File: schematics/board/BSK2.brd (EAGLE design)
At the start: 82 x 100 mm, 26 parts

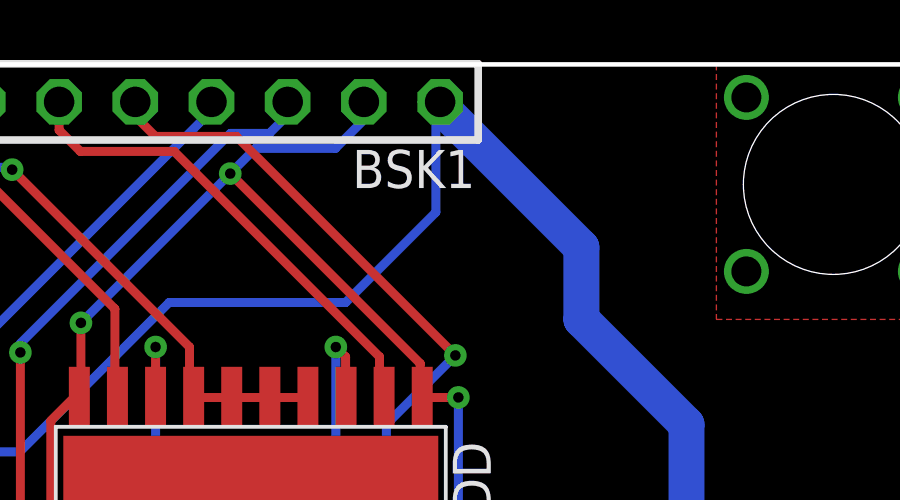
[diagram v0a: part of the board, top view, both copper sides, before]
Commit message: Подписаны разъемы на платах
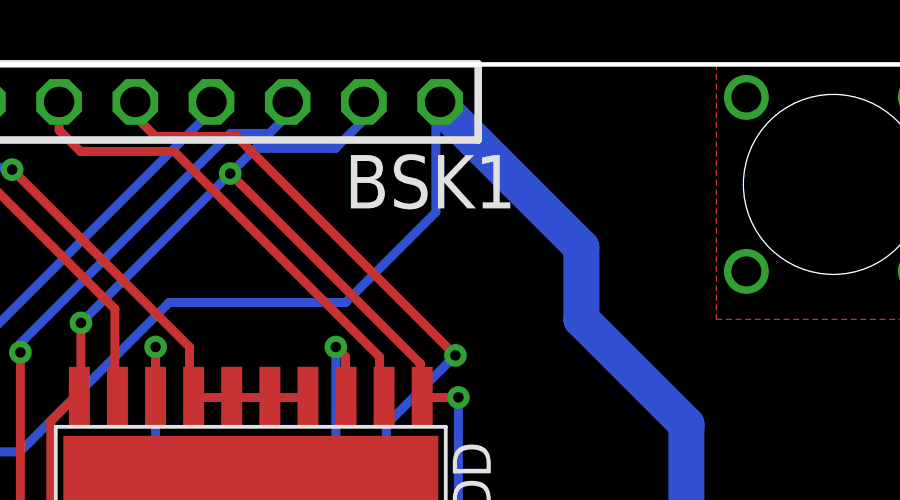
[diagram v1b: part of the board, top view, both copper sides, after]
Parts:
- renumbered BSK1 to TO_BSK1
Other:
- board text added: "BSK1"
- board text added: "to BSK1"
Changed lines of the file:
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@@
 <text x="52.2" y="1.9" size="1.778" layer="26" rot="MR0">BSK2 "Концерн ИТС"</text>
 <circle x="41" y="50" radius="15.25" width="0.2" layer="20"/>
+<text x="54.7" y="95.2" size="1.778" layer="25">BSK1</text>
+<text x="63.5" y="95" size="1.778" layer="26" rot="MR0">to BSK1</text>
 </plain>
 <attributes>
@@
 <attribute name="VALUE" x="23.310459375" y="27.30414375" size="1.27" layer="27" rot="R135"/>
 </element>
-<element name="BSK1" library="pinheadCS" package="1X08" value="" x="49" y="98.75" smashed="yes">
-<attribute name="NAME" x="54.9638" y="95.8788" size="1.27" layer="25" ratio="10"/>
+<element name="TO_BSK1" library="pinheadCS" package="1X08" value="" x="49" y="98.75" smashed="yes">
 <attribute name="VALUE" x="38.84" y="95.575" size="1.27" layer="27"/>
 </element>
@@
 <contactref element="U$8" pad="17"/>
 <contactref element="U$14" pad="67"/>
-<contactref element="BSK1" pad="1"/>
+<contactref element="TO_BSK1" pad="1"/>
 <wire x1="41.6208" y1="86.6346" x2="38.5802" y2="89.6752" width="0.3" layer="1"/>
 <wire x1="41.6208" y1="77.1342" x2="41.6208" y2="86.6346" width="0.3" layer="1"/>
@@
 <contactref element="U$8" pad="11"/>
 <contactref element="U$8" pad="20"/>
-<contactref element="BSK1" pad="7"/>
+<contactref element="TO_BSK1" pad="7"/>
 <contactref element="U$5" pad="3"/>
 <wire x1="57.4548" y1="88.8966" x2="57.295" y2="88.92" width="0.3" layer="1"/>
@@
 <signal name="1W">
 <contactref element="U$5" pad="4"/>
-<contactref element="BSK1" pad="6"/>
+<contactref element="TO_BSK1" pad="6"/>
 <wire x1="35.88" y1="71.875" x2="35.005" y2="71" width="0.3" layer="1"/>
 <wire x1="35.005" y1="71" x2="33.7" y2="71" width="0.3" layer="1"/>
@@
 </signal>
 <signal name="B2_KEM+">
-<contactref element="BSK1" pad="3"/>
+<contactref element="TO_BSK1" pad="3"/>
 <contactref element="U$8" pad="2"/>
 <wire x1="55.8714" y1="89.1228" x2="55.8714" y2="90.2538" width="0.3" layer="1"/>
@@
 </signal>
 <signal name="B2_KEM-">
-<contactref element="BSK1" pad="2"/>
+<contactref element="TO_BSK1" pad="2"/>
 <contactref element="U$8" pad="9"/>
 <wire x1="47.135" y1="88.92" x2="47.0496" y2="89.1228" width="0.3" layer="1"/>
@@
 </signal>
 <signal name="B2_KHEAT">
-<contactref element="BSK1" pad="4"/>
+<contactref element="TO_BSK1" pad="4"/>
 <contactref element="U$8" pad="19"/>
 <wire x1="56.025" y1="79.32" x2="56.025" y2="77.475" width="0.3" layer="1"/>
@@
 </signal>
 <signal name="B2_KVCC">
-<contactref element="BSK1" pad="5"/>
+<contactref element="TO_BSK1" pad="5"/>
 <contactref element="R10" pad="1"/>
 <contactref element="R11" pad="1"/>
@@
 <signal name="BUS+">
 <contactref element="R19" pad="2"/>
-<contactref element="BSK1" pad="8"/>
+<contactref element="TO_BSK1" pad="8"/>
 <contactref element="U$3" pad="1"/>
 <contactref element="U$3" pad="2"/>

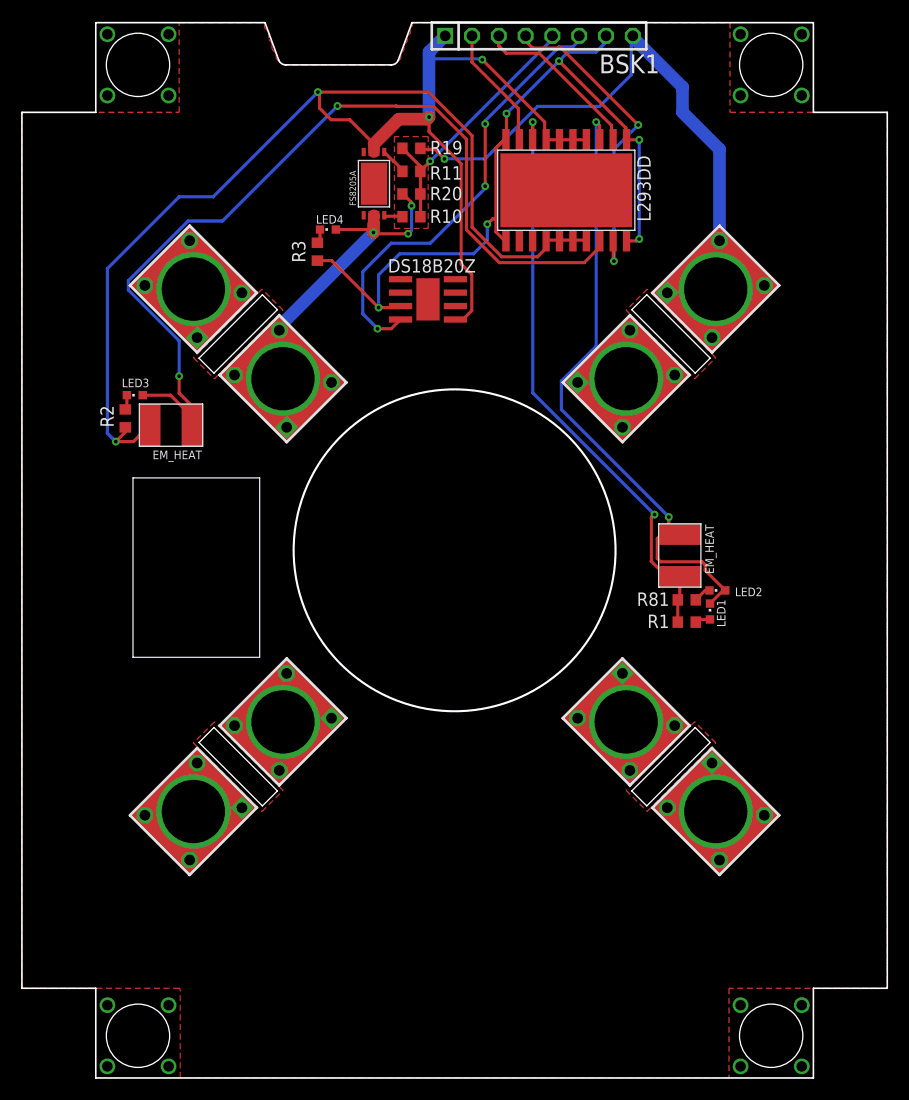
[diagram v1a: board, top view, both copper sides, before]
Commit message: Внёс незначительные правки на платах. Но пока не везде
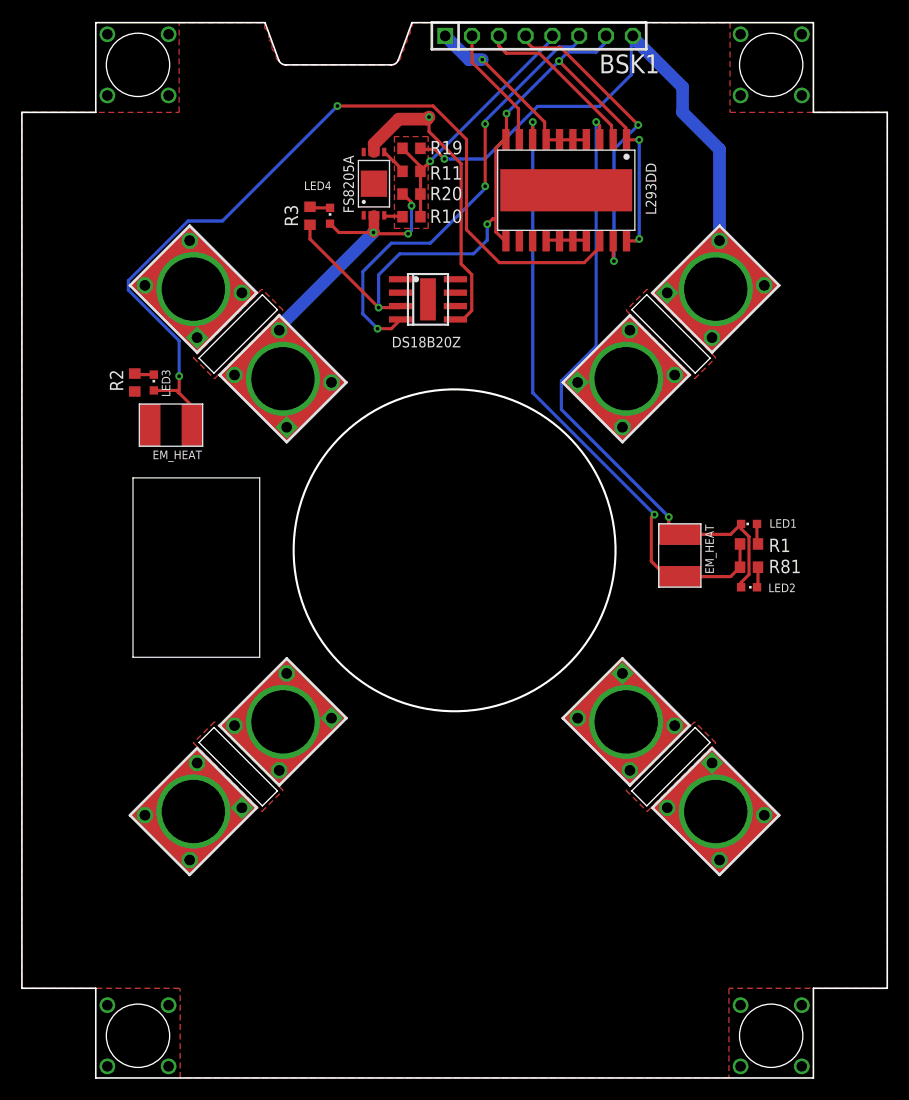
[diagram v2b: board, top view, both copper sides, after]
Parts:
- removed U$14: FS8205A, CanCubeSat:FS8205A
- added FS8205A: FS8205A+, CanCubeSat:FS8205A+
- moved R1 9.46 mm to (68.9, 50.6)
- moved LED1 9.09 mm to (68.9, 52.5), turned to 90 degrees
- moved R81 6.66 mm to (68.9, 48.4)
- moved R2 3.52 mm to (10.7, 65.9)
- moved R3 3.47 mm to (27.3, 81.7)
- moved LED2 3.01 mm to (68.9, 46.5), turned to 270 degrees
- moved LED3 2.16 mm to (12.5, 65.9), turned to 0 degrees
- moved LED4 1.32 mm to (29.2, 81.7), turned to 0 degrees
- renumbered U$5 to DS18B20Z, U$8 to L293DD
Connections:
- removed net HEAT: DS18B20Z.HEAT, L293DD.HEAT, U$14.HEAT
- net BUS-: now also FS8205A.23; no longer U$14.23
- net GND: now also DS18B20Z.HEAT, FS8205A.67, FS8205A.HEAT, L293DD.HEAT; no longer U$14.67
- net N$8: now also FS8205A.4; no longer U$14.4
- net N$9: now also FS8205A.5; no longer U$14.5
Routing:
- net GND: track 151.7 -> 52.2 mm, vias 4 -> 2
- net N$2: track 55.9 -> 59.8 mm
- net N$3: track 86.4 -> 82.6 mm
- net 5V: track 74.8 -> 77.7 mm
- net N$1: track 61.0 -> 59.7 mm
- net BUS-: track 44.6 -> 45.4 mm
- net N$25: track 1.35 -> 1.94 mm
- added copper zone on layer 1, net GND
- removed copper zone on layer 1, net HEAT

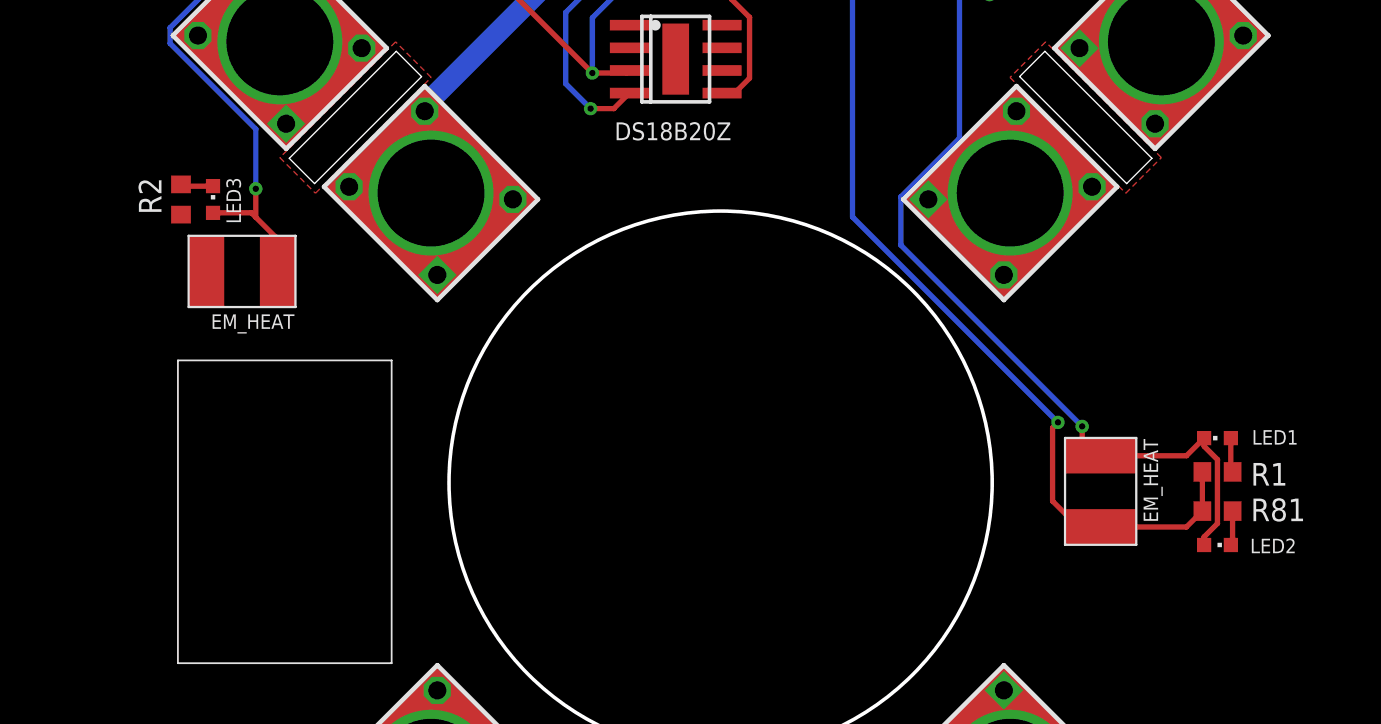
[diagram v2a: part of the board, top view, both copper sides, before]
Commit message: Внесены косметические изменения на БСК2 и БСК3
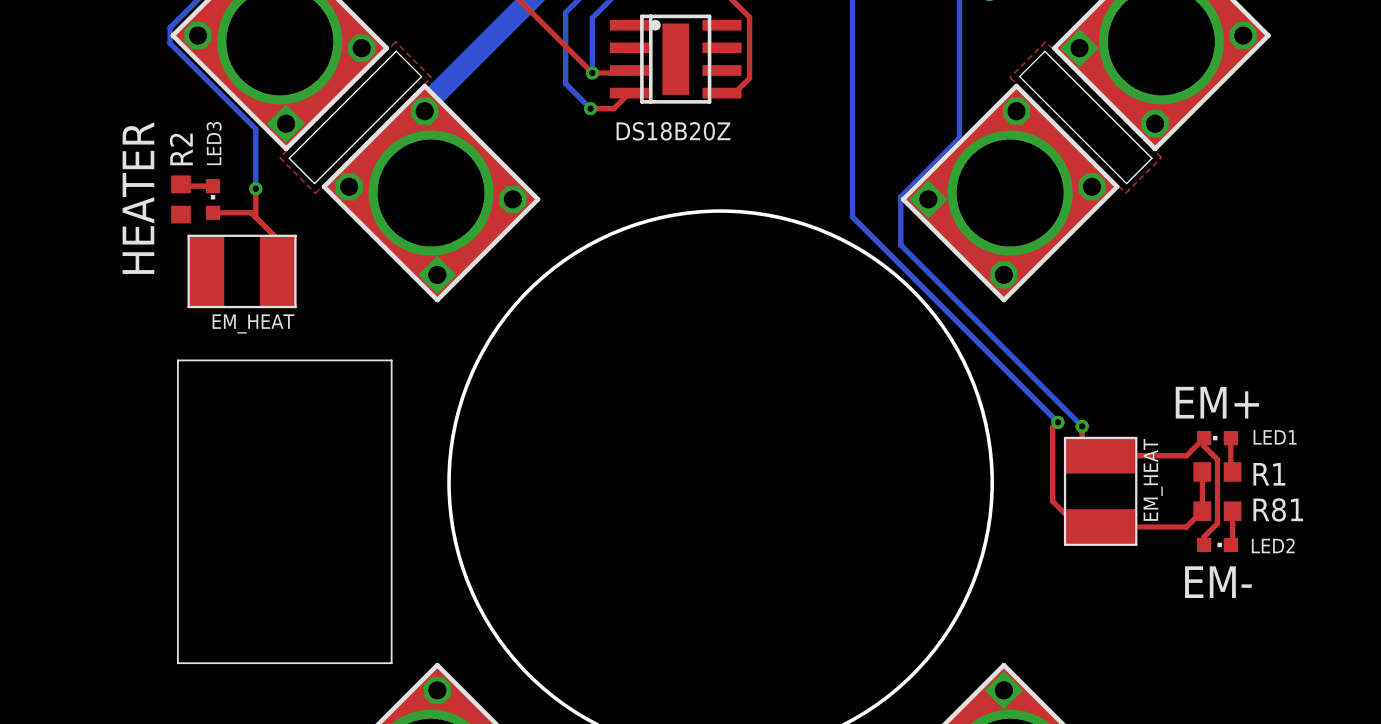
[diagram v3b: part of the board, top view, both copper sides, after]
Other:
- board text added: "EM+"
- board text added: "EM-"
- board text added: "HEATER"
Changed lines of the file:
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@@
 <?xml version="1.0" encoding="utf-8"?>
 <!DOCTYPE eagle SYSTEM "eagle.dtd">
-<eagle version="9.5.1">
+<eagle version="9.4.2">
 <drawing>
 <settings>
@@
 <layer number="14" name="Route14" color="22" fill="1" visible="no" active="no"/>
 <layer number="15" name="Route15" color="23" fill="1" visible="no" active="no"/>
-<layer number="16" name="Bottom" color="1" fill="1" visible="yes" active="yes"/>
+<layer number="16" name="Bottom" color="1" fill="1" visible="no" active="yes"/>
 <layer number="17" name="Pads" color="2" fill="1" visible="yes" active="yes"/>
 <layer number="18" name="Vias" color="2" fill="1" visible="yes" active="yes"/>
@@
 <layer number="20" name="Dimension" color="24" fill="1" visible="yes" active="yes"/>
 <layer number="21" name="tPlace" color="7" fill="1" visible="yes" active="yes"/>
-<layer number="22" name="bPlace" color="7" fill="1" visible="yes" active="yes"/>
+<layer number="22" name="bPlace" color="7" fill="1" visible="no" active="yes"/>
 <layer number="23" name="tOrigins" color="15" fill="1" visible="yes" active="yes"/>
-<layer number="24" name="bOrigins" color="15" fill="1" visible="yes" active="yes"/>
+<layer number="24" name="bOrigins" color="15" fill="1" visible="no" active="yes"/>
 <layer number="25" name="tNames" color="7" fill="1" visible="yes" active="yes"/>
-<layer number="26" name="bNames" color="7" fill="1" visible="yes" active="yes"/>
+<layer number="26" name="bNames" color="7" fill="1" visible="no" active="yes"/>
 <layer number="27" name="tValues" color="7" fill="1" visible="no" active="yes"/>
-<layer number="28" name="bValues" color="7" fill="1" visible="yes" active="yes"/>
-<layer number="29" name="tStop" color="7" fill="3" visible="yes" active="yes"/>
+<layer number="28" name="bValues" color="7" fill="1" visible="no" active="yes"/>
+<layer number="29" name="tStop" color="7" fill="3" visible="no" active="yes"/>
 <layer number="30" name="bStop" color="7" fill="6" visible="no" active="yes"/>
 <layer number="31" name="tCream" color="7" fill="4" visible="no" active="yes"/>
@@
 <layer number="38" name="bTest" color="7" fill="1" visible="no" active="yes"/>
 <layer number="39" name="tKeepout" color="4" fill="11" visible="yes" active="yes"/>
-<layer number="40" name="bKeepout" color="1" fill="11" visible="yes" active="yes"/>
+<layer number="40" name="bKeepout" color="1" fill="11" visible="no" active="yes"/>
 <layer number="41" name="tRestrict" color="4" fill="10" visible="yes" active="yes"/>
-<layer number="42" name="bRestrict" color="1" fill="10" visible="yes" active="yes"/>
-<layer number="43" name="vRestrict" color="2" fill="10" visible="yes" active="yes"/>
+<layer number="42" name="bRestrict" color="1" fill="10" visible="no" active="yes"/>
+<layer number="43" name="vRestrict" color="2" fill="10" visible="no" active="yes"/>
 <layer number="44" name="Drills" color="7" fill="1" visible="no" active="yes"/>
-<layer number="45" name="Holes" color="7" fill="1" visible="yes" active="yes"/>
+<layer number="45" name="Holes" color="7" fill="1" visible="no" active="yes"/>
 <layer number="46" name="Milling" color="3" fill="1" visible="no" active="yes"/>
 <layer number="47" name="Measures" color="7" fill="1" visible="no" active="yes"/>
-<layer number="48" name="Document" color="7" fill="1" visible="yes" active="yes"/>
-<layer number="49" name="Reference" color="7" fill="1" visible="yes" active="yes"/>
+<layer number="48" name="Document" color="7" fill="1" visible="no" active="yes"/>
+<layer number="49" name="Reference" color="7" fill="1" visible="no" active="yes"/>
 <layer number="51" name="tDocu" color="7" fill="1" visible="yes" active="yes"/>
-<layer number="52" name="bDocu" color="7" fill="1" visible="yes" active="yes"/>
+<layer number="52" name="bDocu" color="7" fill="1" visible="no" active="yes"/>
 <layer number="88" name="SimResults" color="9" fill="1" visible="no" active="no"/>
 <layer number="89" name="SimProbes" color="9" fill="1" visible="no" active="no"/>
@@
 <layer number="98" name="Guide" color="6" fill="1" visible="no" active="no"/>
 <layer number="99" name="SpiceOrder" color="5" fill="1" visible="no" active="no"/>
-<layer number="100" name="DocFrame" color="15" fill="1" visible="yes" active="yes"/>
-<layer number="101" name="NotChangedData" color="15" fill="1" visible="yes" active="yes"/>
-<layer number="102" name="ChangedData" color="15" fill="1" visible="yes" active="yes"/>
+<layer number="100" name="DocFrame" color="15" fill="1" visible="no" active="yes"/>
+<layer number="101" name="NotChangedData" color="15" fill="1" visible="no" active="yes"/>
+<layer number="102" name="ChangedData" color="15" fill="1" visible="no" active="yes"/>
 </layers>
 <board>
@@
 <text x="54.7" y="95.2" size="1.778" layer="25">BSK1</text>
 <text x="63.5" y="95" size="1.778" layer="26" rot="MR0">to BSK1</text>
+<text x="68.9" y="53.6" size="1.778" layer="21" align="bottom-center">EM+</text>
+<text x="68.9" y="45.3" size="1.778" layer="21" align="top-center">EM-</text>
+<text x="9.2" y="65.9" size="1.778" layer="21" rot="R90" align="bottom-center">HEATER</text>
 </plain>
 <attributes>
@@
 </element>
 <element name="R2" library="resistor" library_urn="urn:adsk.eagle:library:348" package="R0603" package3d_urn="urn:adsk.eagle:package:23555/3" value="2k" x="10.7" y="65.9" smashed="yes" rot="R270">
-<attribute name="NAME" x="8.335" y="67.135" size="1.27" layer="25" rot="R270"/>
+<attribute name="NAME" x="11.365" y="67.665" size="1.27" layer="25" rot="R90"/>
 <attribute name="VALUE" x="8.795" y="66.535" size="1.27" layer="27" rot="R270"/>
 </element>
 <element name="LED3" library="led" library_urn="urn:adsk.eagle:library:259" package="CHIPLED_0603" package3d_urn="urn:adsk.eagle:package:15822/2" value="" x="12.5" y="65.9" smashed="yes">
-<attribute name="NAME" x="14.065" y="64.53" size="0.8128" layer="25" rot="R90"/>
+<attribute name="NAME" x="12.965" y="67.73" size="0.8128" layer="25" rot="R90"/>
 <attribute name="POPULARITY" value="28" x="-9.2" y="56.7" size="1.778" layer="27" display="off"/>
 <attribute name="VALUE" x="14.405" y="64.63" size="1.27" layer="27" rot="R90"/>

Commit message: Платы подготовлены для Резонита
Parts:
- renumbered TO_BSK1 to BSK1
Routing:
- net GND: track 52.2 -> 111.7 mm
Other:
- board text added: "BUS"
- board text removed: "BSK1"
